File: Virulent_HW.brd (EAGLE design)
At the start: 16 parts

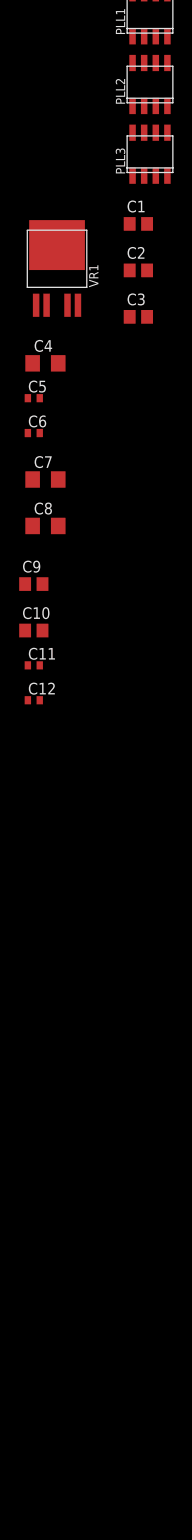
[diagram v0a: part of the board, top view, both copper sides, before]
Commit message: Added RGB LED (MSL0201RGB) and Hex Inverter (SN74ACT14) to library. Updated PLL circuitry in schematic.
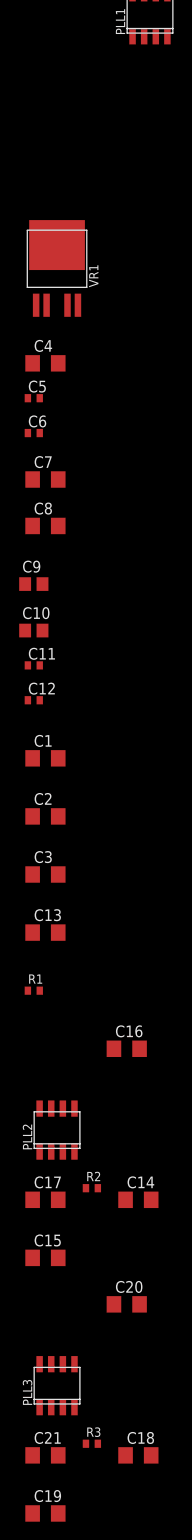
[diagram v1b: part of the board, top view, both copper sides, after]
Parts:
- added C13: 1n, rcl:C1206
- added C14, C15, C18, C19: (no value), rcl:C1206
- added C16, C20: 1u, rcl:C1206
- added C17: 5.6n, rcl:C1206
- added C21: 1.8n, rcl:C1206
- added R1: 470k, Virulent_HW:R0402
- added R2: 56k, Virulent_HW:R0402
- added R3: 100k, Virulent_HW:R0402
- C1, C2: device rcl:C0805 -> rcl:C1206
- C3: value (none) -> 1u; device rcl:C0805 -> rcl:C1206
- moved PLL3 135.0 mm to (-17.8, -166.4)
- moved PLL2 114.8 mm to (-17.8, -138.4)
- moved C3 61.8 mm to (-19.1, -110.5)
- moved C2 60.5 mm to (-19.1, -104.1)
- moved C1 59.3 mm to (-19.1, -97.8)
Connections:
- new net N$1: C1.1, PLL1.1
- new net N$10: C17.1, PLL2.5, R2.1
- new net N$12: C18.1, PLL3.1
- new net N$13: PLL3.6, R3.2
- new net N$14: C19.1, PLL3.2
- new net N$15: PLL3.8
- new net N$17: C21.1, PLL3.5, R3.1
- new net N$2: C14.1, PLL2.1
- new net N$3: PLL1.6, R1.2
- new net N$4: C13.1, PLL1.5, R1.1
- new net N$5: C2.1, PLL1.2
- new net N$6: PLL1.8
- new net N$7: PLL2.6, R2.2
- new net N$8: C15.1, PLL2.2
- new net N$9: PLL2.8
- new net NFC_OUT: PLL1.3, PLL2.3, PLL3.3
- net +5V: now also C16.1, C20.1, C3.1, PLL1.4, PLL2.4, PLL3.4
- net GND: now also C1.2, C13.2, C14.2, C15.2, C16.2, C17.2, C18.2, C19.2, C2.2, C20.2, C21.2, C3.2, PLL1.7, PLL2.7, PLL3.7
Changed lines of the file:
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@@
 <elements>
 <element name="PLL1" library="Virulent_HW" package="SOIC-8" value="LM567CM/NOPB-ND" x="-7.62" y="-16.51"/>
-<element name="PLL2" library="Virulent_HW" package="SOIC-8" value="LM567CM/NOPB-ND" x="-7.62" y="-24.13"/>
-<element name="PLL3" library="Virulent_HW" package="SOIC-8" value="LM567CM/NOPB-ND" x="-7.62" y="-31.75"/>
-<element name="C1" library="rcl" package="C0805" value="" x="-8.89" y="-39.37"/>
-<element name="C2" library="rcl" package="C0805" value="" x="-8.89" y="-44.45"/>
-<element name="C3" library="rcl" package="C0805" value="" x="-8.89" y="-49.53"/>
 <element name="VR1" library="motorFeedback" package="PG-TO252-5-11" value="TLE4476D" x="-17.78" y="-43.18"/>
 <element name="C4" library="rcl" package="C1206" value="0.47u" x="-19.05" y="-54.61"/>
@@
 <element name="C11" library="rcl" package="C0402" value="0.01u" x="-20.32" y="-87.63"/>
 <element name="C12" library="rcl" package="C0402" value="0.1u" x="-20.32" y="-91.44"/>
+<element name="C1" library="rcl" package="C1206" value="" x="-19.05" y="-97.79"/>
+<element name="C2" library="rcl" package="C1206" value="" x="-19.05" y="-104.14"/>
+<element name="C3" library="rcl" package="C1206" value="1u" x="-19.05" y="-110.49"/>
+<element name="C13" library="rcl" package="C1206" value="1n" x="-19.05" y="-116.84"/>
+<element name="R1" library="Virulent_HW" package="R0402" value="470k" x="-20.32" y="-123.19"/>
+<element name="PLL2" library="Virulent_HW" package="SOIC-8" value="LM567CM/NOPB-ND" x="-17.78" y="-138.43"/>
+<element name="C14" library="rcl" package="C1206" value="" x="-8.89" y="-146.05"/>
+<element name="C15" library="rcl" package="C1206" value="" x="-19.05" y="-152.4"/>
+<element name="C16" library="rcl" package="C1206" value="1u" x="-10.16" y="-129.54"/>
+<element name="C17" library="rcl" package="C1206" value="5.6n" x="-19.05" y="-146.05"/>
+<element name="R2" library="Virulent_HW" package="R0402" value="56k" x="-13.97" y="-144.78"/>
+<element name="PLL3" library="Virulent_HW" package="SOIC-8" value="LM567CM/NOPB-ND" x="-17.78" y="-166.37"/>
+<element name="C18" library="rcl" package="C1206" value="" x="-8.89" y="-173.99"/>
+<element name="C19" library="rcl" package="C1206" value="" x="-19.05" y="-180.34"/>
+<element name="C20" library="rcl" package="C1206" value="1u" x="-10.16" y="-157.48"/>
+<element name="C21" library="rcl" package="C1206" value="1.8n" x="-19.05" y="-173.99"/>
+<element name="R3" library="Virulent_HW" package="R0402" value="100k" x="-13.97" y="-172.72"/>
 </elements>
 <signals>
@@
 <contactref element="C7" pad="1"/>
 <contactref element="C5" pad="1"/>
+<contactref element="PLL1" pad="4"/>
+<contactref element="C3" pad="1"/>
+<contactref element="PLL2" pad="4"/>
+<contactref element="C16" pad="1"/>
+<contactref element="PLL3" pad="4"/>
+<contactref element="C20" pad="1"/>
+<wire x1="-11.56" y1="-157.48" x2="-15.875" y2="-168.7195" width="0" layer="19" extent="1-1"/>
+<wire x1="-15.875" y1="-140.7795" x2="-11.56" y2="-157.48" width="0" layer="19" extent="1-1"/>
+<wire x1="-11.56" y1="-129.54" x2="-15.875" y2="-140.7795" width="0" layer="19" extent="1-1"/>
+<wire x1="-20.45" y1="-110.49" x2="-11.56" y2="-129.54" width="0" layer="19" extent="1-1"/>
+<wire x1="-20.45" y1="-67.31" x2="-20.45" y2="-110.49" width="0" layer="19" extent="1-1"/>
 <wire x1="-20.97" y1="-58.42" x2="-20.45" y2="-67.31" width="0" layer="19" extent="1-1"/>
 <wire x1="-16.637" y1="-48.26" x2="-20.97" y2="-58.42" width="0" layer="19" extent="1-1"/>
+<wire x1="-5.715" y1="-18.8595" x2="-16.637" y2="-48.26" width="0" layer="19" extent="1-1"/>
 </signal>
 <signal name="+9-36V">
@@
 <contactref element="C10" pad="2"/>
 <contactref element="C12" pad="2"/>
+<contactref element="C1" pad="2"/>
+<contactref element="C13" pad="2"/>
+<contactref element="C3" pad="2"/>
+<contactref element="C2" pad="2"/>
+<contactref element="PLL1" pad="7"/>
+<contactref element="C14" pad="2"/>
+<contactref element="C17" pad="2"/>
+<contactref element="C16" pad="2"/>
+<contactref element="C15" pad="2"/>
+<contactref element="PLL2" pad="7"/>
+<contactref element="C18" pad="2"/>
+<contactref element="C21" pad="2"/>
+<contactref element="C20" pad="2"/>
+<contactref element="C19" pad="2"/>
+<contactref element="PLL3" pad="7"/>
+<wire x1="-17.65" y1="-173.99" x2="-17.65" y2="-180.34" width="0" layer="19" extent="1-1"/>
+<wire x1="-18.415" y1="-164.0205" x2="-17.65" y2="-173.99" width="0" layer="19" extent="1-1"/>
+<wire x1="-7.49" y1="-173.99" x2="-17.65" y2="-173.99" width="0" layer="19" extent="1-1"/>
+<wire x1="-17.65" y1="-152.4" x2="-18.415" y2="-164.0205" width="0" layer="19" extent="1-1"/>
+<wire x1="-17.65" y1="-146.05" x2="-17.65" y2="-152.4" width="0" layer="19" extent="1-1"/>
+<wire x1="-18.415" y1="-136.0805" x2="-17.65" y2="-146.05" width="0" layer="19" extent="1-1"/>
+<wire x1="-7.49" y1="-146.05" x2="-17.65" y2="-146.05" width="0" layer="19" extent="1-1"/>
+<wire x1="-8.76" y1="-157.48" x2="-17.65" y2="-152.4" width="0" layer="19" extent="1-1"/>
+<wire x1="-8.76" y1="-129.54" x2="-18.415" y2="-136.0805" width="0" layer="19" extent="1-1"/>
+<wire x1="-17.65" y1="-116.84" x2="-8.76" y2="-129.54" width="0" layer="19" extent="1-1"/>
+<wire x1="-17.65" y1="-110.49" x2="-17.65" y2="-116.84" width="0" layer="19" extent="1-1"/>
+<wire x1="-17.65" y1="-104.14" x2="-17.65" y2="-110.49" width="0" layer="19" extent="1-1"/>
+<wire x1="-17.65" y1="-97.79" x2="-17.65" y2="-104.14" width="0" layer="19" extent="1-1"/>
+<wire x1="-19.67" y1="-91.44" x2="-17.65" y2="-97.79" width="0" layer="19" extent="1-1"/>
 <wire x1="-19.67" y1="-87.63" x2="-19.67" y2="-91.44" width="0" layer="19" extent="1-1"/>
 <wire x1="-19.37" y1="-83.82" x2="-19.67" y2="-87.63" width="0" layer="19" extent="1-1"/>
@@
 <wire x1="-17.65" y1="-54.61" x2="-19.67" y2="-58.42" width="0" layer="19" extent="1-1"/>
 <wire x1="-17.78" y1="-41.6814" x2="-17.65" y2="-54.61" width="0" layer="19" extent="1-1"/>
+<wire x1="-8.255" y1="-14.1605" x2="-17.78" y2="-41.6814" width="0" layer="19" extent="1-1"/>
 </signal>
 <signal name="5V_ENABLE">
 <contactref element="VR1" pad="5"/>
 </signal>
+<signal name="N$1">
+<contactref element="PLL1" pad="1"/>
+<contactref element="C1" pad="1"/>
+<wire x1="-9.525" y1="-18.8595" x2="-20.45" y2="-97.79" width="0" layer="19" extent="1-1"/>
+</signal>
+<signal name="N$3">
+<contactref element="PLL1" pad="6"/>
+<contactref element="R1" pad="2"/>
+<wire x1="-6.985" y1="-14.1605" x2="-19.67" y2="-123.19" width="0" layer="19" extent="1-1"/>
+</signal>
+<signal name="N$5">
+<contactref element="C2" pad="1"/>
+<contactref element="PLL1" pad="2"/>
+<wire x1="-8.255" y1="-18.8595" x2="-20.45" y2="-104.14" width="0" layer="19" extent="1-1"/>
+</signal>
+<signal name="N$6">
+<contactref element="PLL1" pad="8"/>
+</signal>
+<signal name="N$4">
+<contactref element="R1" pad="1"/>
+<contactref element="C13" pad="1"/>
+<contactref element="PLL1" pad="5"/>
+<wire x1="-20.45" y1="-116.84" x2="-20.97" y2="-123.19" width="0" layer="19" extent="1-1"/>
+<wire x1="-5.715" y1="-14.1605" x2="-20.45" y2="-116.84" width="0" layer="19" extent="1-1"/>
+</signal>
+<signal name="NFC_OUT">
+<contactref element="PLL1" pad="3"/>
+<contactref element="PLL2" pad="3"/>
+<contactref element="PLL3" pad="3"/>
+<wire x1="-17.145" y1="-140.7795" x2="-17.145" y2="-168.7195" width="0" layer="19" extent="1-1"/>
+<wire x1="-6.985" y1="-18.8595" x2="-17.145" y2="-140.7795" width="0" layer="19" extent="1-1"/>
+</signal>
+<signal name="N$2">
+<contactref element="PLL2" pad="1"/>
+<contactref element="C14" pad="1"/>
+<wire x1="-10.29" y1="-146.05" x2="-19.685" y2="-140.7795" width="0" layer="19" extent="1-1"/>
+</signal>
+<signal name="N$7">
+<contactref element="PLL2" pad="6"/>
+<contactref element="R2" pad="2"/>
+<wire x1="-17.145" y1="-136.0805" x2="-13.32" y2="-144.78" width="0" layer="19" extent="1-1"/>
+</signal>
+<signal name="N$8">
+<contactref element="C15" pad="1"/>
+<contactref element="PLL2" pad="2"/>
+<wire x1="-18.415" y1="-140.7795" x2="-20.45" y2="-152.4" width="0" layer="19" extent="1-1"/>
+</signal>
+<signal name="N$9">
+<contactref element="PLL2" pad="8"/>
+</signal>
+<signal name="N$10">
+<contactref element="R2" pad="1"/>
+<contactref element="C17" pad="1"/>
+<contactref element="PLL2" pad="5"/>
+<wire x1="-14.62" y1="-144.78" x2="-20.45" y2="-146.05" width="0" layer="19" extent="1-1"/>
+<wire x1="-15.875" y1="-136.0805" x2="-14.62" y2="-144.78" width="0" layer="19" extent="1-1"/>
+</signal>
+<signal name="N$12">
+<contactref element="PLL3" pad="1"/>
+<contactref element="C18" pad="1"/>
+<wire x1="-10.29" y1="-173.99" x2="-19.685" y2="-168.7195" width="0" layer="19" extent="1-1"/>
+</signal>
+<signal name="N$13">
+<contactref element="PLL3" pad="6"/>
+<contactref element="R3" pad="2"/>
+<wire x1="-17.145" y1="-164.0205" x2="-13.32" y2="-172.72" width="0" layer="19" extent="1-1"/>
+</signal>
+<signal name="N$14">
+<contactref element="C19" pad="1"/>
+<contactref element="PLL3" pad="2"/>
+<wire x1="-18.415" y1="-168.7195" x2="-20.45" y2="-180.34" width="0" layer="19" extent="1-1"/>
+</signal>
+<signal name="N$15">
+<contactref element="PLL3" pad="8"/>
+</signal>
+<signal name="N$17">
+<contactref element="R3" pad="1"/>
+<contactref element="C21" pad="1"/>
+<contactref element="PLL3" pad="5"/>
+<wire x1="-14.62" y1="-172.72" x2="-20.45" y2="-173.99" width="0" layer="19" extent="1-1"/>
+<wire x1="-15.875" y1="-164.0205" x2="-14.62" y2="-172.72" width="0" layer="19" extent="1-1"/>
+</signal>
 </signals>

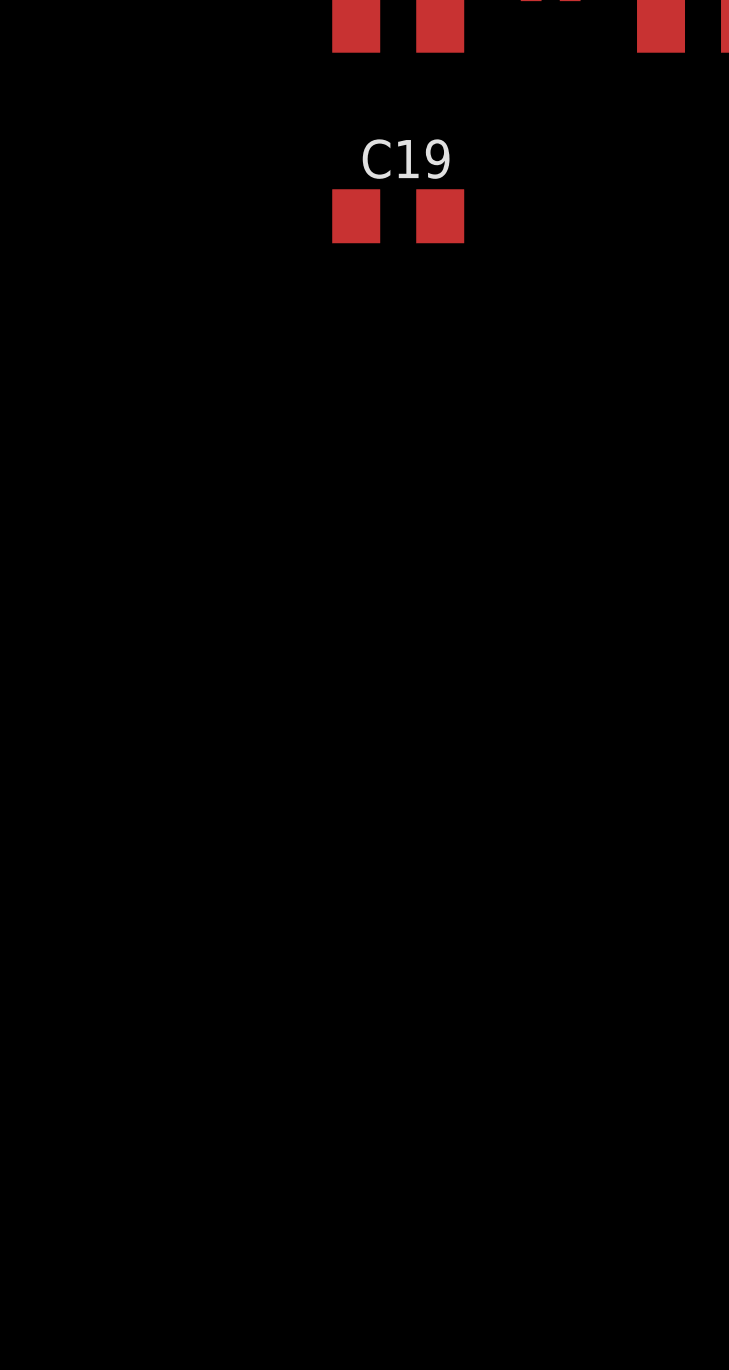
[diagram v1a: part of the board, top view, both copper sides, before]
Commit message: Added crystal oscillator to library. Added carrier frequency circuitry to schematic.
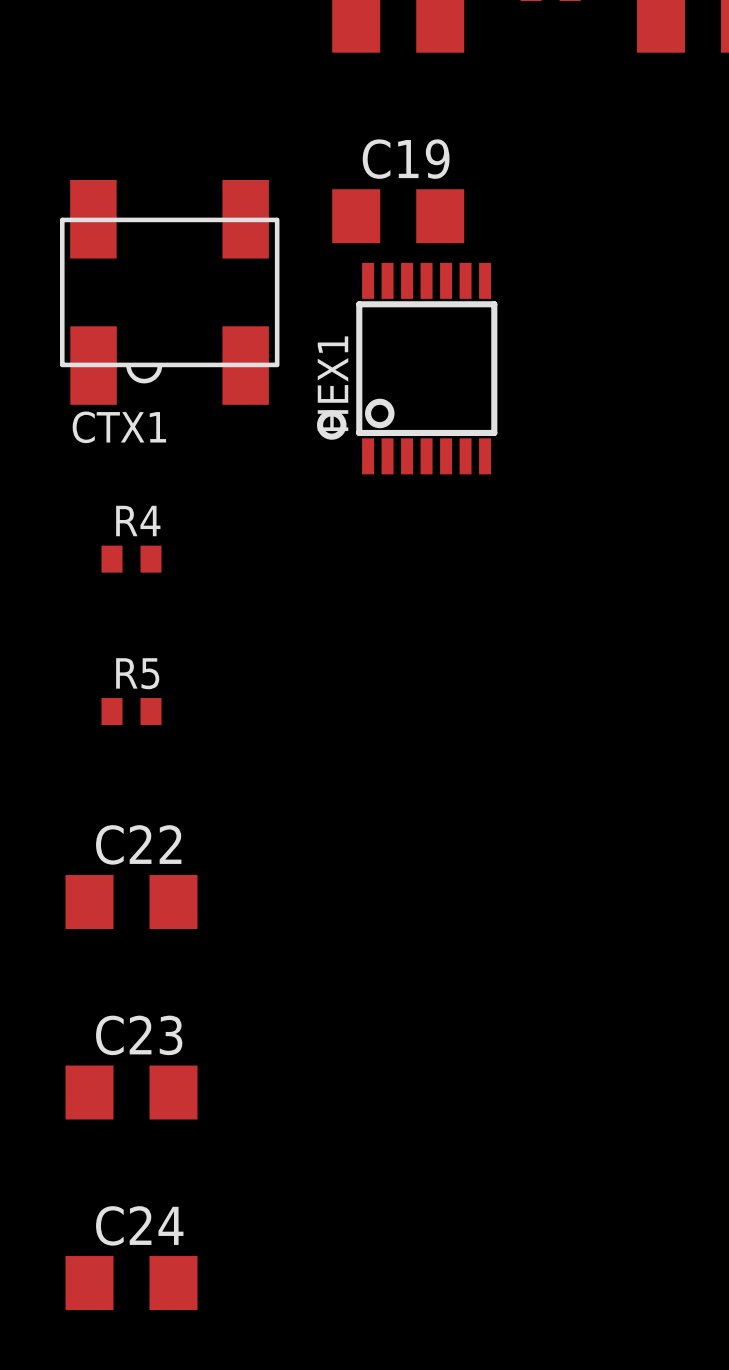
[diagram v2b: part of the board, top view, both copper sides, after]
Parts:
- added C22, C23: 15p, rcl:C1206
- added C24: 10n, rcl:C1206
- added CTX1: 405C11A13M5600\4-SMD, Virulent_HW:4-SMD
- added HEX1: SN74ACT14PW, Virulent_HW:TSSOP14
- added R4: 100k, Virulent_HW:R0402
- added R5: 150k, Virulent_HW:R0402
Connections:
- new net CARRIER_FREQ: HEX1.10, HEX1.12, HEX1.2, HEX1.4, HEX1.6
- new net N$18: C23.1, CTX1.1, HEX1.9, R4.2
- new net N$19: HEX1.8, R4.1, R5.2
- new net N$20: C22.2, CTX1.3, R5.1
- new net N$24: HEX1.1, HEX1.11, HEX1.13, HEX1.3, HEX1.5
- net +5V: now also C24.1, HEX1.14
- net GND: now also C22.1, C23.2, C24.2, CTX1.2, CTX1.4, HEX1.7
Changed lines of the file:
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@@
 <element name="C21" library="rcl" package="C1206" value="1.8n" x="-19.05" y="-173.99"/>
 <element name="R3" library="Virulent_HW" package="R0402" value="100k" x="-13.97" y="-172.72"/>
+<element name="HEX1" library="Virulent_HW" package="TSSOP14" value="SN74ACT14PW" x="-17.78" y="-185.42"/>
+<element name="CTX1" library="Virulent_HW" package="4-SMD" value="405C11A13M5600\4-SMD" x="-26.67" y="-182.88"/>
+<element name="R4" library="Virulent_HW" package="R0402" value="100k" x="-27.94" y="-191.77"/>
+<element name="R5" library="Virulent_HW" package="R0402" value="150k" x="-27.94" y="-196.85"/>
+<element name="C22" library="rcl" package="C1206" value="15p" x="-27.94" y="-203.2"/>
+<element name="C23" library="rcl" package="C1206" value="15p" x="-27.94" y="-209.55"/>
+<element name="C24" library="rcl" package="C1206" value="10n" x="-27.94" y="-215.9"/>
 </elements>
 <signals>
@@
 <contactref element="PLL3" pad="4"/>
 <contactref element="C20" pad="1"/>
+<contactref element="HEX1" pad="14"/>
+<contactref element="C24" pad="1"/>
+<wire x1="-20.055" y1="-182.495" x2="-29.34" y2="-215.9" width="0" layer="19" extent="1-1"/>
+<wire x1="-15.875" y1="-168.7195" x2="-20.055" y2="-182.495" width="0" layer="19" extent="1-1"/>
 <wire x1="-11.56" y1="-157.48" x2="-15.875" y2="-168.7195" width="0" layer="19" extent="1-1"/>
 <wire x1="-15.875" y1="-140.7795" x2="-11.56" y2="-157.48" width="0" layer="19" extent="1-1"/>
@@
 <contactref element="C19" pad="2"/>
 <contactref element="PLL3" pad="7"/>
+<contactref element="CTX1" pad="4"/>
+<contactref element="CTX1" pad="2"/>
+<contactref element="C23" pad="2"/>
+<contactref element="C22" pad="1"/>
+<contactref element="C24" pad="2"/>
+<contactref element="HEX1" pad="7"/>
+<wire x1="-26.54" y1="-209.55" x2="-26.54" y2="-215.9" width="0" layer="19" extent="1-1"/>
+<wire x1="-29.34" y1="-203.2" x2="-26.54" y2="-209.55" width="0" layer="19" extent="1-1"/>
+<wire x1="-24.1352" y1="-185.3184" x2="-29.34" y2="-203.2" width="0" layer="19" extent="1-1"/>
+<wire x1="-29.21" y1="-180.4416" x2="-24.1352" y2="-185.3184" width="0" layer="19" extent="1-1"/>
+<wire x1="-17.65" y1="-180.34" x2="-24.1352" y2="-185.3184" width="0" layer="19" extent="1-1"/>
 <wire x1="-17.65" y1="-173.99" x2="-17.65" y2="-180.34" width="0" layer="19" extent="1-1"/>
+<wire x1="-16.155" y1="-188.345" x2="-17.65" y2="-180.34" width="0" layer="19" extent="1-1"/>
 <wire x1="-18.415" y1="-164.0205" x2="-17.65" y2="-173.99" width="0" layer="19" extent="1-1"/>
 <wire x1="-7.49" y1="-173.99" x2="-17.65" y2="-173.99" width="0" layer="19" extent="1-1"/>
@@
 <wire x1="-15.875" y1="-164.0205" x2="-14.62" y2="-172.72" width="0" layer="19" extent="1-1"/>
 </signal>
+<signal name="N$18">
+<contactref element="CTX1" pad="1"/>
+<contactref element="C23" pad="1"/>
+<contactref element="R4" pad="2"/>
+<contactref element="HEX1" pad="9"/>
+<wire x1="-27.29" y1="-191.77" x2="-29.34" y2="-209.55" width="0" layer="19" extent="1-1"/>
+<wire x1="-29.2048" y1="-185.3184" x2="-27.29" y2="-191.77" width="0" layer="19" extent="1-1"/>
+<wire x1="-16.805" y1="-182.495" x2="-29.2048" y2="-185.3184" width="0" layer="19" extent="1-1"/>
+</signal>
+<signal name="N$19">
+<contactref element="R4" pad="1"/>
+<contactref element="R5" pad="2"/>
+<contactref element="HEX1" pad="8"/>
+<wire x1="-28.59" y1="-191.77" x2="-27.29" y2="-196.85" width="0" layer="19" extent="1-1"/>
+<wire x1="-16.155" y1="-182.495" x2="-28.59" y2="-191.77" width="0" layer="19" extent="1-1"/>
+</signal>
+<signal name="N$20">
+<contactref element="R5" pad="1"/>
+<contactref element="CTX1" pad="3"/>
+<contactref element="C22" pad="2"/>
+<wire x1="-28.59" y1="-196.85" x2="-26.54" y2="-203.2" width="0" layer="19" extent="1-1"/>
+<wire x1="-24.1352" y1="-180.4416" x2="-28.59" y2="-196.85" width="0" layer="19" extent="1-1"/>
+</signal>
+<signal name="CARRIER_FREQ">
+<contactref element="HEX1" pad="10"/>
+<contactref element="HEX1" pad="12"/>
+<contactref element="HEX1" pad="6"/>
+<contactref element="HEX1" pad="2"/>
+<contactref element="HEX1" pad="4"/>
+<wire x1="-18.105" y1="-188.345" x2="-19.405" y2="-188.345" width="0" layer="19" extent="1-1"/>
+<wire x1="-16.805" y1="-188.345" x2="-18.105" y2="-188.345" width="0" layer="19" extent="1-1"/>
+<wire x1="-18.755" y1="-182.495" x2="-19.405" y2="-188.345" width="0" layer="19" extent="1-1"/>
+<wire x1="-17.455" y1="-182.495" x2="-18.755" y2="-182.495" width="0" layer="19" extent="1-1"/>
+</signal>
+<signal name="N$24">
+<contactref element="HEX1" pad="11"/>
+<contactref element="HEX1" pad="13"/>
+<contactref element="HEX1" pad="5"/>
+<contactref element="HEX1" pad="1"/>
+<contactref element="HEX1" pad="3"/>
+<wire x1="-18.755" y1="-188.345" x2="-20.055" y2="-188.345" width="0" layer="19" extent="1-1"/>
+<wire x1="-17.455" y1="-188.345" x2="-18.755" y2="-188.345" width="0" layer="19" extent="1-1"/>
+<wire x1="-18.105" y1="-182.495" x2="-18.755" y2="-188.345" width="0" layer="19" extent="1-1"/>
+<wire x1="-19.405" y1="-182.495" x2="-18.105" y2="-182.495" width="0" layer="19" extent="1-1"/>
+</signal>
 </signals>
